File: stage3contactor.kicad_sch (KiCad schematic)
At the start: 9 parts, among them J10 Screw_Terminal_01x02, J11 Screw_Terminal_01x02, J12 Screw_Terminal_01x02, J14 Screw_Terminal_01x02, J5 Screw_Terminal_01x02, J6 Screw_Terminal_01x02, J7 Screw_Terminal_01x02, J8 Screw_Terminal_01x02, J9 Screw_Terminal_01x02

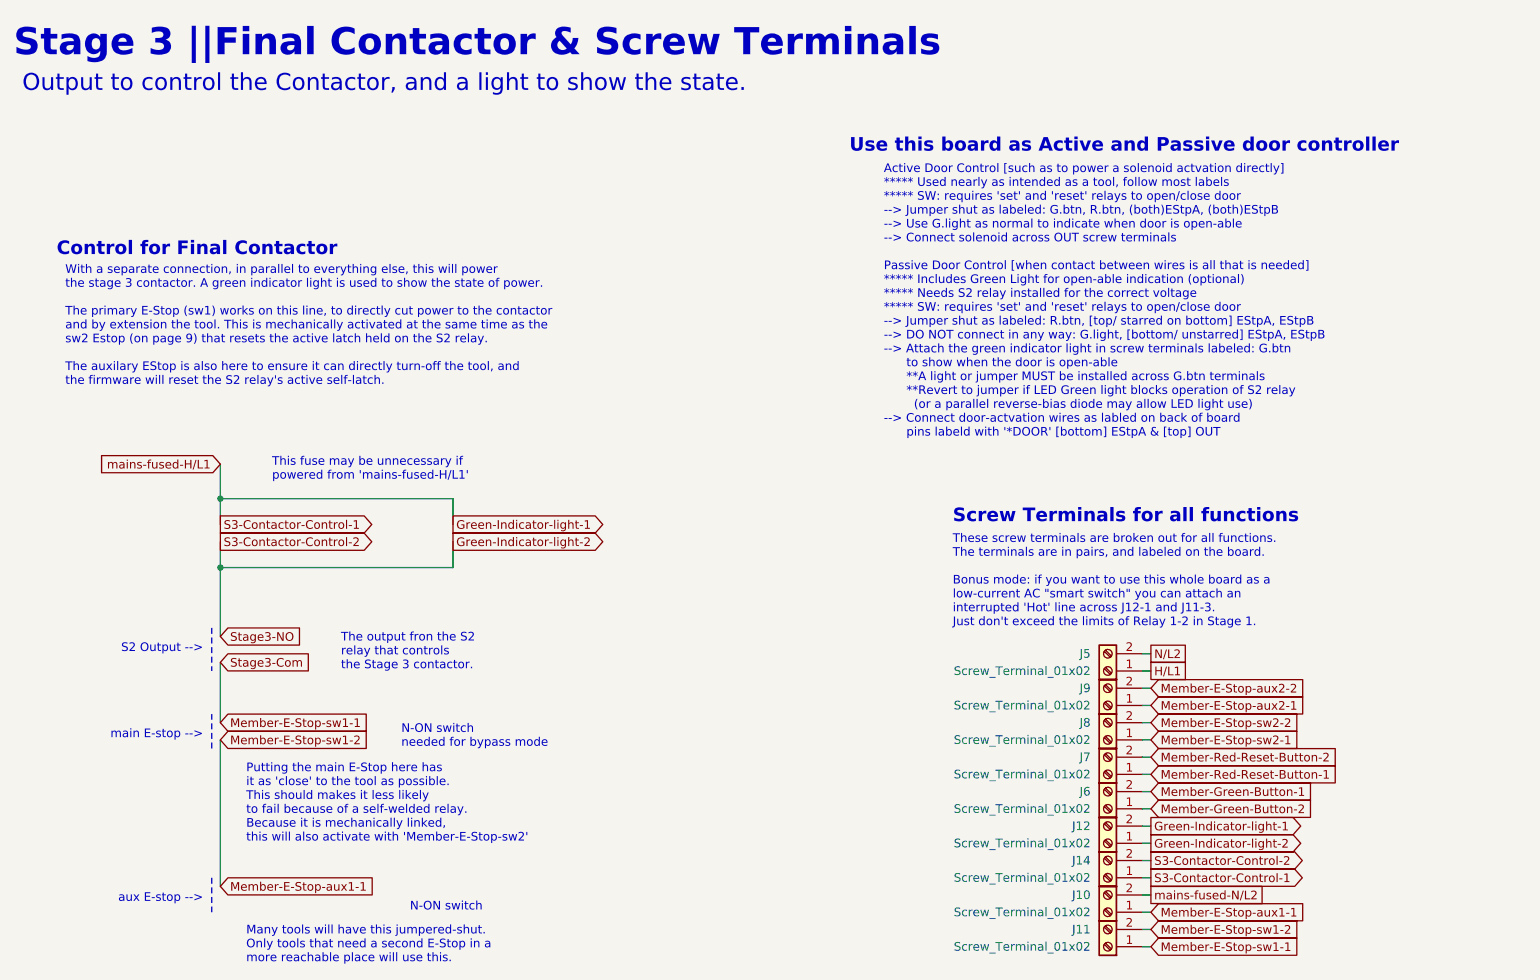
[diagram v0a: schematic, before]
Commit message: double-check mains connections, update notes
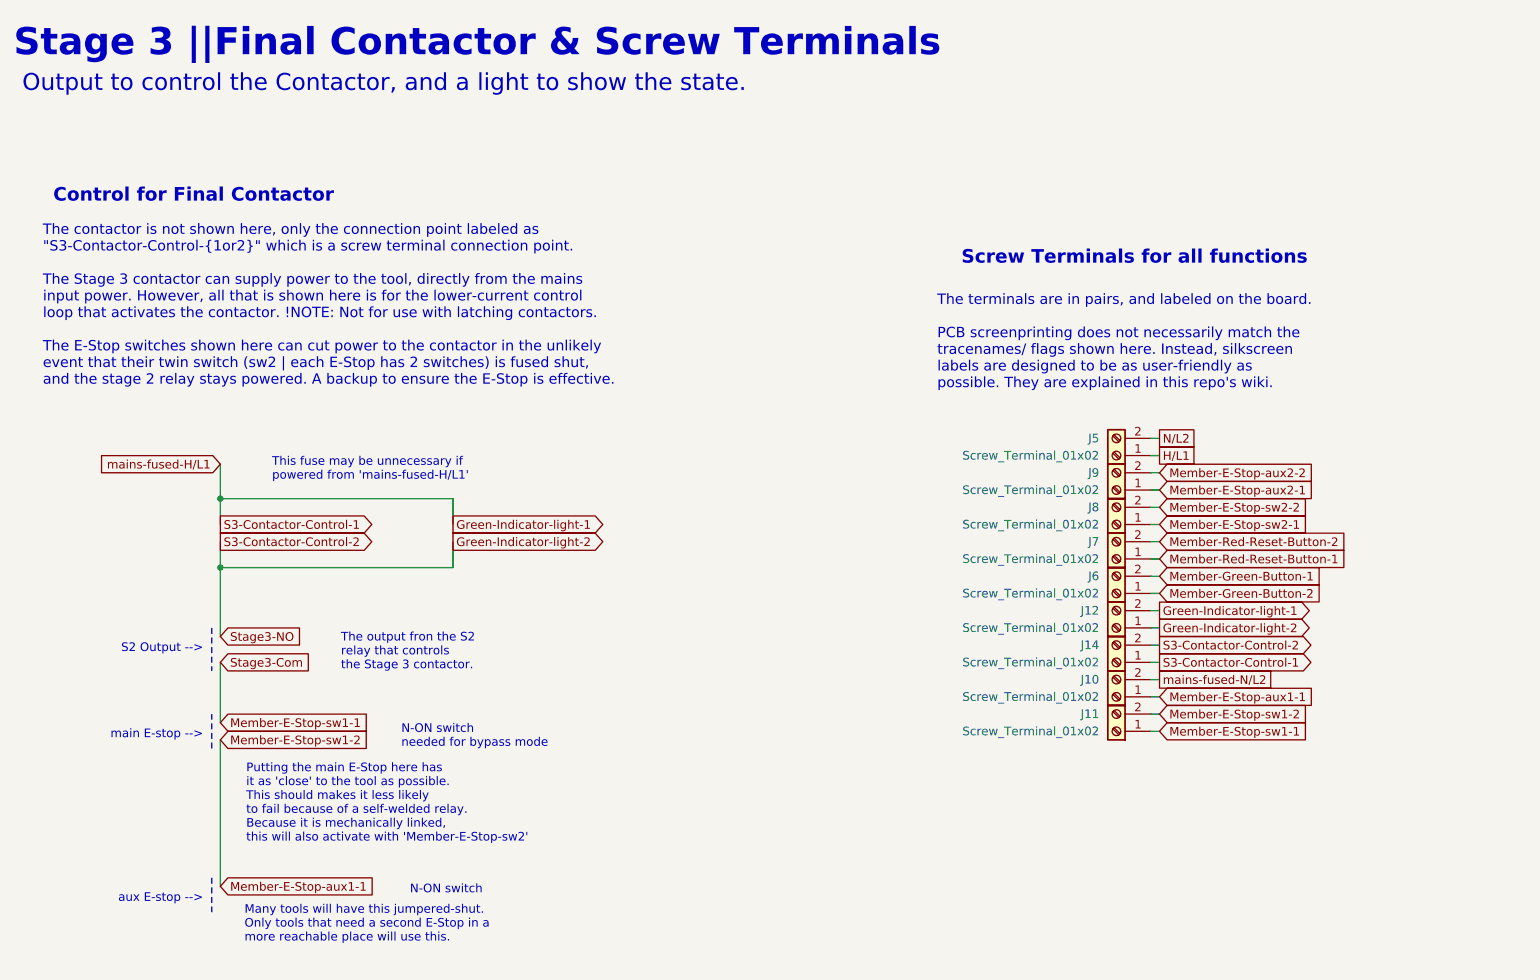
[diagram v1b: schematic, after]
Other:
- note added: "The contactor is not shown here, only the connection point labeled as "S3-Contactor-Control-{1or2}" which is a screw terminal connection point. The Stage 3 contactor can supply power to the tool, directly from the mains input power. However, all that is shown here is for the lower-current control loop that activates the contactor. !NOTE: Not for use with latching contactors. The E-Stop switches s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"
- note added: "The terminals are in pairs, and labeled on the board. PCB screenprinting does not necessarily match the tracenames/ flags shown here. Instead, silkscreen labels are designed to be as user-friendly as possible. They are explained in this repo's wiki."
- note removed: "Active Door Control [such as to power a solenoid actvation directly] ***** Used nearly as intended as a tool, follow most labels ***** SW: requires 'set' and 'reset' relays to open/close door --> Jumper shut as labeled: G.btn, R.btn, (both)EStpA, (both)EStpB --> Use G.light as normal to indicate when door is open-able --> Connect solenoid across OUT screw terminals Passive Door Control [when cont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"
- note removed: "These screw terminals are broken out for all functions. The terminals are in pairs, and labeled on the board. Bonus mode: if you want to use this whole board as a low-current AC "smart switch" you can attach an interrupted 'Hot' line across J12-1 and J11-3. Just don't exceed the limits of Relay 1-2 in Stage 1."
- note removed: "Use this board as Active and Passive door controller"
- note removed: "With a separate connection, in parallel to everything else, this will power the stage 3 contactor. A green indicator light is used to show the state of power. The primary E-Stop (sw1) works on this line, to directly cut power to the contactor and by extension the tool. This is mechanically activated at the same time as the sw2 Estop (on page 9) that resets the active latch held on the S2 relay. T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"
- moved on the sheet: J10, J11, J12, J14, J5, J6, J7, J8, J9

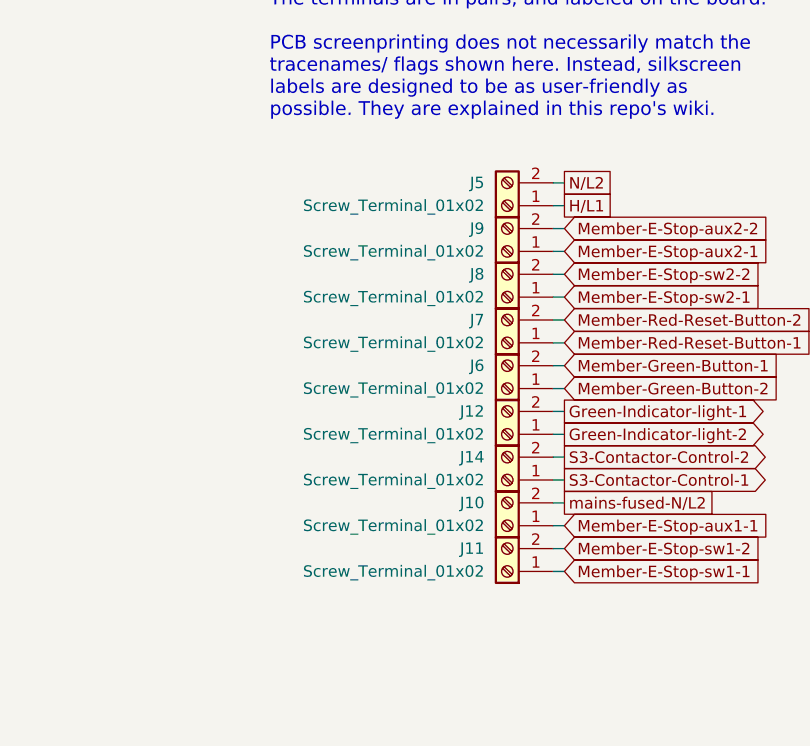
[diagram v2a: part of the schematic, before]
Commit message: placed new screw terminals on board
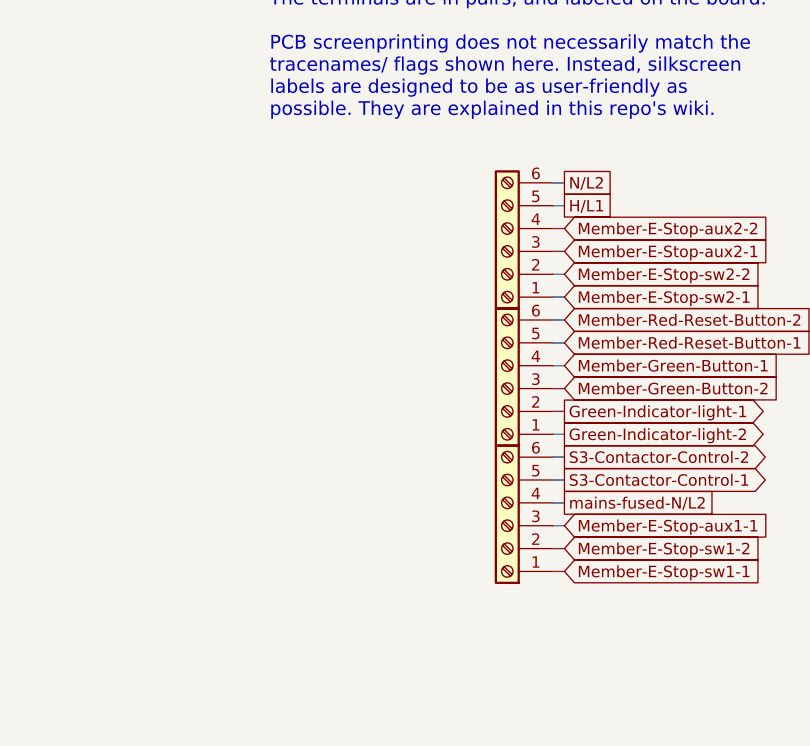
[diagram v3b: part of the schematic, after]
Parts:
- removed J10, J11, J12, J14, J5, J6, J7, J8, J9: Screw_Terminal_01x02, TerminalBlock:TerminalBlock_Altech_AK300-2_P5.00mm, symbol Connector:Screw_Terminal_01x02
- added J1, J17, J18: Screw_Terminal_01x06, screw_terminal:CONN-TH_6P-P5.00_MX128-5.0-06P-GN01-CU-Y-A, symbol Connector:Screw_Terminal_01x06
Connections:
- net Green-Indicator-light-1: now also J17.2 (Pin_2), J18.5 (Pin_5)
- net Green-Indicator-light-2: now also J17.1 (Pin_1), J18.6 (Pin_6)
- net H/L1: now also J1.5 (Pin_5)
- net Member-E-Stop-aux1-1: now also J18.2 (Pin_2), J18.3 (Pin_3)
- net Member-E-Stop-aux2-1: now also J1.3 (Pin_3)
- net Member-E-Stop-aux2-2: now also J1.4 (Pin_4)
- net Member-E-Stop-sw1-1: now also J18.1 (Pin_1)
- net Member-E-Stop-sw2-1: now also J1.1 (Pin_1)
- net Member-E-Stop-sw2-2: now also J1.2 (Pin_2)
- net Member-Green-Button-1: now also J17.4 (Pin_4)
- net Member-Green-Button-2: now also J17.3 (Pin_3)
- net Member-Red-Reset-Button-1: now also J17.5 (Pin_5)
- net Member-Red-Reset-Button-2: now also J17.6 (Pin_6)
- net N/L2: now also J1.6 (Pin_6)
- net mains-fused-N/L2: now also J18.4 (Pin_4)

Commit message: save lcsc part number
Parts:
- J1, J17, J18: lcsc_id (none) -> C5290371
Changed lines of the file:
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@@
+			)
+		)
+		(property "lcsc_id" "C5290371"
+			(at 198.12 93.98 0)
+			(effects
+				(font
+					(size 1.27 1.27)
+				)
+				(hide yes)
 			)
 		)
@@
 			)
 		)
+		(property "lcsc_id" "C5290371"
+			(at 198.12 109.22 0)
+			(effects
+				(font
+					(size 1.27 1.27)
+				)
+				(hide yes)
+			)
+		)
 		(pin "4"
 		)
@@
 			(at 198.12 124.46 0)
 			(effects
+				(font
+					(size 1.27 1.27)
+				)
+				(hide yes)
+			)
+		)
+		(property "lcsc_id" "C5290371"
+			(at 198.12 124.46 0)
+			(effects

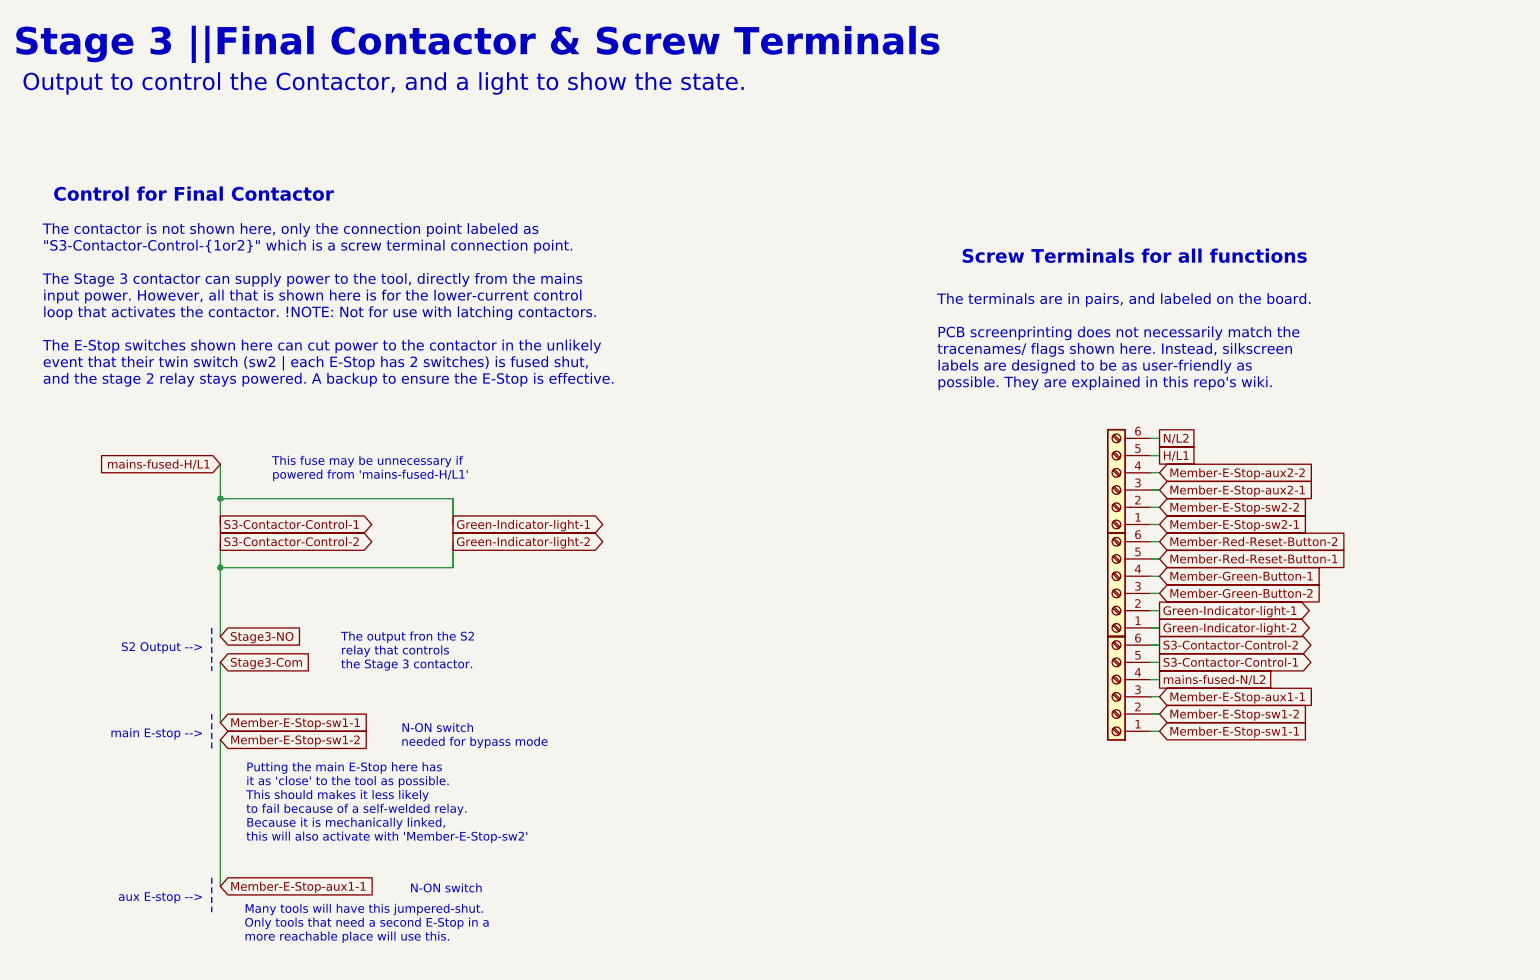
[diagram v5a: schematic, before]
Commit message: moved LED GPIO to fit free pins for ethernet wing
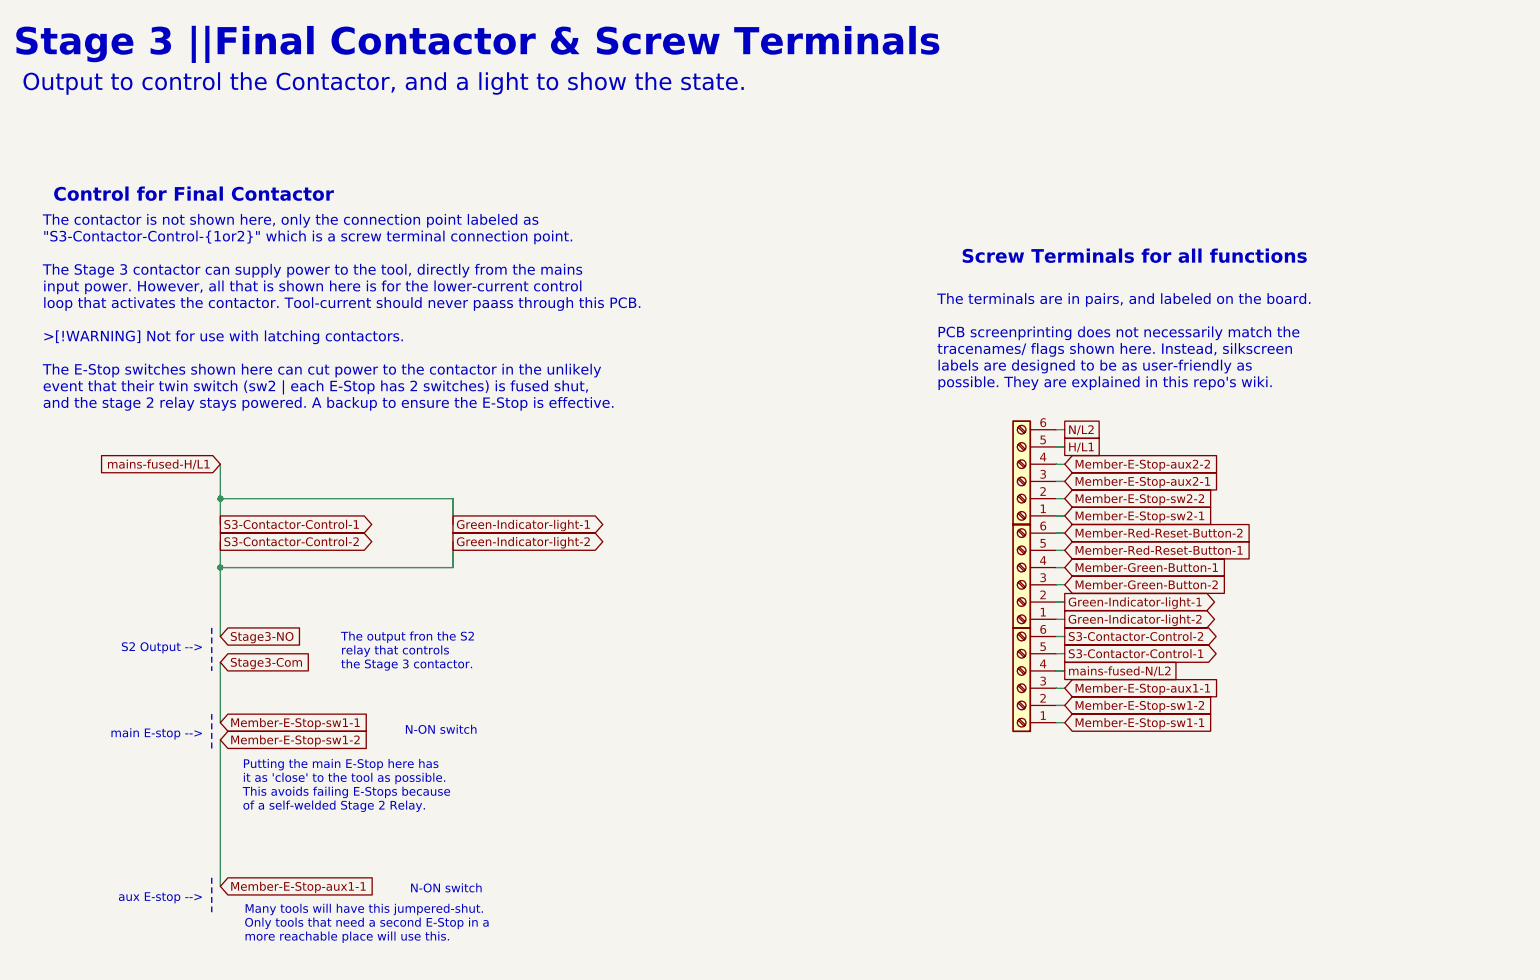
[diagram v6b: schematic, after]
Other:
- note added: "Putting the main E-Stop here has it as 'close' to the tool as possible. This avoids failing E-Stops because of a self-welded Stage 2 Relay."
- note added: "The contactor is not shown here, only the connection point labeled as "S3-Contactor-Control-{1or2}" which is a screw terminal connection point. The Stage 3 contactor can supply power to the tool, directly from the mains input power. However, all that is shown here is for the lower-current control loop that activates the contactor. Tool-current should never paass through this PCB. >[!WARNING] Not 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"
- note removed: "N-ON switch needed for bypass mode"
- note removed: "Putting the main E-Stop here has it as 'close' to the tool as possible. This should makes it less likely to fail because of a self-welded relay. Because it is mechanically linked, this will also activate with 'Member-E-Stop-sw2'"
- note removed: "The contactor is not shown here, only the connection point labeled as "S3-Contactor-Control-{1or2}" which is a screw terminal connection point. The Stage 3 contactor can supply power to the tool, directly from the mains input power. However, all that is shown here is for the lower-current control loop that activates the contactor. !NOTE: Not for use with latching contactors. The E-Stop switches s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"
- note removed: "This fuse may be unnecessary if powered from 'mains-fused-H/L1'"

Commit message: 1.4.1 schematic update
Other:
- note added: "EStop-aux1-2"
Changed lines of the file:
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@@
+		)
+	)
+	(text "EStop-aux1-2"
+		(exclude_from_sim no)
+		(at 210.566 121.666 0)
+		(effects
+			(font
+				(size 1.524 1.524)
+			)
+			(justify left bottom)
 		)
 	)

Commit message: update reference values for better ibom
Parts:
- renumbered J1 to J20, J17 to J21, J18 to J22
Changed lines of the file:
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@@
 		(dnp no)
 		(fields_autoplaced yes)
-		(property "Reference" "J1"
+		(property "Reference" "J20"
 			(at 184.15 78.74 0)
 			(effects
@@
 			(project ""
 				(path "/586efc0f-7de2-49a7-ac21-ecfef2f716d6/6f44f9bb-3a88-498d-9739-be3794f35f17/7e35b9a1-6df7-4aff-8cae-346c220af792"
-					(reference "J1")
+					(reference "J20")
 					(unit 1)
 				)
@@
 		(dnp no)
 		(fields_autoplaced yes)
-		(property "Reference" "J17"
+		(property "Reference" "J21"
 			(at 184.15 93.98 0)
 			(effects
@@
 			(project "wing-combo"
 				(path "/586efc0f-7de2-49a7-ac21-ecfef2f716d6/6f44f9bb-3a88-498d-9739-be3794f35f17/7e35b9a1-6df7-4aff-8cae-346c220af792"
-					(reference "J17")
+					(reference "J21")
 					(unit 1)
 				)
@@
 		(dnp no)
 		(fields_autoplaced yes)
-		(property "Reference" "J18"
+		(property "Reference" "J22"
 			(at 184.15 109.22 0)
 			(effects
@@
 			(project "wing-combo"
 				(path "/586efc0f-7de2-49a7-ac21-ecfef2f716d6/6f44f9bb-3a88-498d-9739-be3794f35f17/7e35b9a1-6df7-4aff-8cae-346c220af792"
-					(reference "J18")
+					(reference "J22")
 					(unit 1)
 				)
